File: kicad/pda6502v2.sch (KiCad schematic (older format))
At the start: 85 parts, among them J1 GPIO1, J2 GPIO2, J3 UART, J4 Screw_Terminal_01x02, J5 Conn_02x04_Odd_Even, J6 ICSP, J7 SPI, J8 FPGA_EXT, J9 SID, SW1 SW_Push, U1 W65C02SxP, U10 LT3030, U11 SC28L92A1B, U2 W65C22SxP, U3 W65C22SxP, U4 DS1818, U5 AS6C4008-55PCN, U6 ARMSID, U7 AT25M01, U8 ICE40HX4K-TQ144, U9 TLV1117-33, X1 8 MHz, X2 3.6864 MHz

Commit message: Routing WIP; UART
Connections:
- net UART_RXA~IRQ: now also U8.98 (IOR_148); no longer U8.99 (IOR_152)
- net UART_TXA~IRQ: now also U8.97 (IOR_147); no longer U8.98 (IOR_148)
- net UART_~CS: now also U8.99 (IOR_152); no longer U8.97 (IOR_147)
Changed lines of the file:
@@
 Text Label 11750 5550 2    50   ~ 0
 UART_TXB~IRQ
-Text Label 11750 6050 2    50   ~ 0
+Text Label 11750 5950 2    50   ~ 0
 UART_TXA~IRQ
 Text Label 11750 5650 2    50   ~ 0
 UART_RXB~IRQ
-Text Label 11750 6150 2    50   ~ 0
+Text Label 11750 6050 2    50   ~ 0
 UART_RXA~IRQ
 Text Label 11750 5750 2    50   ~ 0
@@
 Text Label 14750 4950 2    50   ~ 0
 RAM_~CS
-Text Label 11750 5950 2    50   ~ 0
+Text Label 11750 6150 2    50   ~ 0
 UART_~CS
 Text Label 11750 6750 2    50   ~ 0

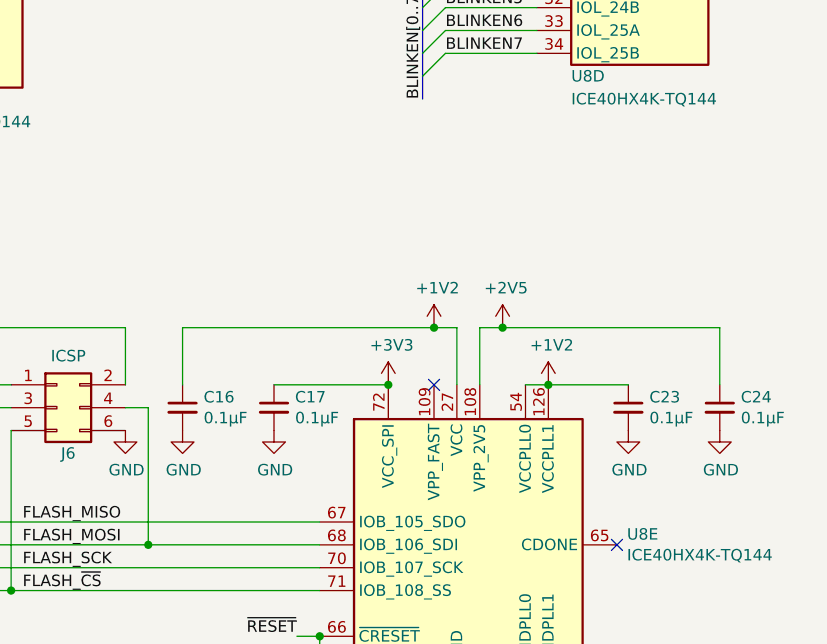
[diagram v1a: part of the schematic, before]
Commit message: LDO placement/routing, XO HandSolder footprint, etc.
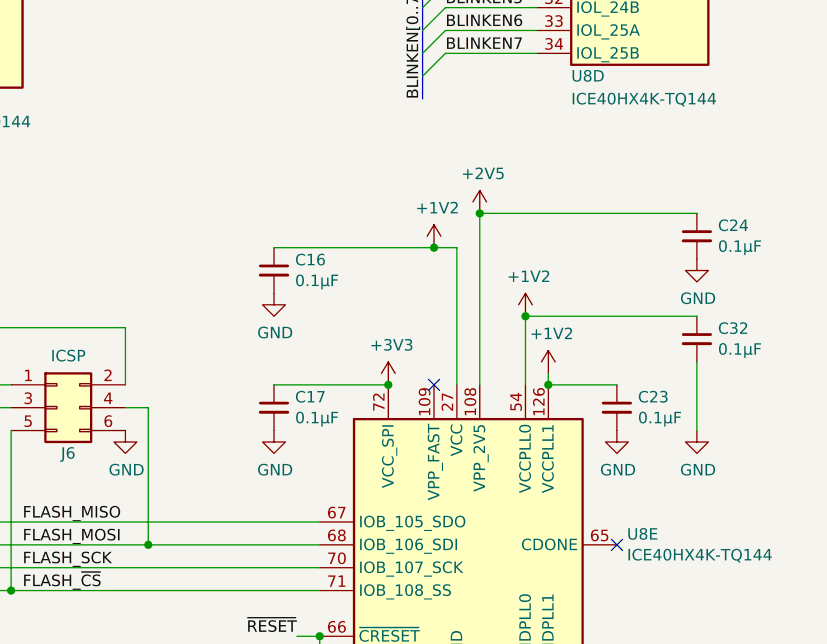
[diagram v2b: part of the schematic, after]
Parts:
- added C32: 0.1μF, Capacitor_SMD:C_0805_2012Metric_Pad1.18x1.45mm_HandSolder, symbol Device:C_Small
- X1, X2: footprint Oscillator:Oscillator_SMD_EuroQuartz_XO53-4Pin_5.0x3.2mm -> pda6502v2:Oscillator_SMD_5.0x3.2mm_HandSolder
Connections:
- net +1V2: now also C32.1
- net GND: now also C32.2
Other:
- moved on the sheet: C16, C23, C24
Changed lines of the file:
@@
 UART_IM
 Wire Wire Line
-	14600 7850 15550 7850
-Wire Wire Line
-	15550 7850 15550 8100
-Wire Wire Line
-	13200 7850 14300 7850
-Wire Wire Line
-	13200 7850 13200 8100
+	14500 7350 15450 7350
+Wire Wire Line
+	13600 7500 14300 7500
 $Comp
 L power:GND #PWR079
 U 1 1 61F81ED6
-P 15550 8300
-F 0 "#PWR079" H 15550 8050 50  0001 C CNN
-F 1 "GND" H 15555 8127 50  0000 C CNN
-F 2 "" H 15550 8300 50  0001 C CNN
-F 3 "" H 15550 8300 50  0001 C CNN
-	1    15550 8300
+P 15450 7550
+F 0 "#PWR079" H 15450 7300 50  0001 C CNN
+F 1 "GND" H 15455 7377 50  0000 C CNN
+F 2 "" H 15450 7550 50  0001 C CNN
+F 3 "" H 15450 7550 50  0001 C CNN
+	1    15450 7550
 	1    0    0    -1
 $EndComp
@@
 L Device:C_Small C24
 U 1 1 61F81ECC
-P 15550 8200
-F 0 "C24" H 15642 8246 50  0000 L CNN
-F 1 "0.1μF" H 15642 8155 50  0000 L CNN
-F 2 "Capacitor_SMD:C_0805_2012Metric_Pad1.18x1.45mm_HandSolder" H 15550 8200 50  0001 C CNN
-F 3 "~" H 15550 8200 50  0001 C CNN
-	1    15550 8200
-	1    0    0    -1
-$EndComp
-Connection ~ 14600 7850
-Connection ~ 14300 7850
-Wire Wire Line
-	14400 7850 14300 7850
-Wire Wire Line
-	14400 8100 14400 7850
-Wire Wire Line
-	14500 7850 14600 7850
-Wire Wire Line
-	14500 8100 14500 7850
-Wire Wire Line
-	14800 8100 15150 8100
+P 15450 7450
+F 0 "C24" H 15542 7496 50  0000 L CNN
+F 1 "0.1μF" H 15542 7405 50  0000 L CNN
+F 2 "Capacitor_SMD:C_0805_2012Metric_Pad1.18x1.45mm_HandSolder" H 15450 7450 50  0001 C CNN
+F 3 "~" H 15450 7450 50  0001 C CNN
+	1    15450 7450
+	1    0    0    -1
+$EndComp
+Connection ~ 14500 7350
+Connection ~ 14300 7500
+Wire Wire Line
+	14400 7500 14300 7500
+Wire Wire Line
+	14400 8100 14400 7500
+Wire Wire Line
+	14500 8100 14500 7350
 $Comp
 L power:GND #PWR077
 U 1 1 61D7E730
-P 15150 8300
-F 0 "#PWR077" H 15150 8050 50  0001 C CNN
-F 1 "GND" H 15155 8127 50  0000 C CNN
-F 2 "" H 15150 8300 50  0001 C CNN
-F 3 "" H 15150 8300 50  0001 C CNN
-	1    15150 8300
+P 15100 8300
+F 0 "#PWR077" H 15100 8050 50  0001 C CNN
+F 1 "GND" H 15105 8127 50  0000 C CNN
+F 2 "" H 15100 8300 50  0001 C CNN
+F 3 "" H 15100 8300 50  0001 C CNN
+	1    15100 8300
 	1    0    0    -1
 $EndComp
@@
 L Device:C_Small C23
 U 1 1 61D7E726
-P 15150 8200
-F 0 "C23" H 15242 8246 50  0000 L CNN
-F 1 "0.1μF" H 15242 8155 50  0000 L CNN
-F 2 "Capacitor_SMD:C_0805_2012Metric_Pad1.18x1.45mm_HandSolder" H 15150 8200 50  0001 C CNN
-F 3 "~" H 15150 8200 50  0001 C CNN
-	1    15150 8200
-	1    0    0    -1
-$EndComp
-Connection ~ 14800 8100
-Wire Wire Line
-	14700 8100 14800 8100
+P 15100 8200
+F 0 "C23" H 15192 8246 50  0000 L CNN
+F 1 "0.1μF" H 15192 8155 50  0000 L CNN
+F 2 "Capacitor_SMD:C_0805_2012Metric_Pad1.18x1.45mm_HandSolder" H 15100 8200 50  0001 C CNN
+F 3 "~" H 15100 8200 50  0001 C CNN
+	1    15100 8200
+	1    0    0    -1
+$EndComp
 $Comp
 L power:GND #PWR060
 U 1 1 61C44B47
-P 13200 8300
-F 0 "#PWR060" H 13200 8050 50  0001 C CNN
-F 1 "GND" H 13205 8127 50  0000 C CNN
-F 2 "" H 13200 8300 50  0001 C CNN
-F 3 "" H 13200 8300 50  0001 C CNN
-	1    13200 8300
+P 13600 7700
+F 0 "#PWR060" H 13600 7450 50  0001 C CNN
+F 1 "GND" H 13605 7527 50  0000 C CNN
+F 2 "" H 13600 7700 50  0001 C CNN
+F 3 "" H 13600 7700 50  0001 C CNN
+	1    13600 7700
 	1    0    0    -1
 $EndComp
@@
 L Device:C_Small C16
 U 1 1 61C44B3D
-P 13200 8200
-F 0 "C16" H 13292 8246 50  0000 L CNN
-F 1 "0.1μF" H 13292 8155 50  0000 L CNN
-F 2 "Capacitor_SMD:C_0805_2012Metric_Pad1.18x1.45mm_HandSolder" H 13200 8200 50  0001 C CNN
-F 3 "~" H 13200 8200 50  0001 C CNN
-	1    13200 8200
+P 13600 7600
+F 0 "C16" H 13692 7646 50  0000 L CNN
+F 1 "0.1μF" H 13692 7555 50  0000 L CNN
+F 2 "Capacitor_SMD:C_0805_2012Metric_Pad1.18x1.45mm_HandSolder" H 13600 7600 50  0001 C CNN
+F 3 "~" H 13600 7600 50  0001 C CNN
+	1    13600 7600
 	1    0    0    -1
 $EndComp
@@
 L power:+1V2 #PWR?
 U 1 1 609BB90F
-P 14800 8100
+P 14800 8050
 AR Path="/609162A8/609BB90F" Ref="#PWR?"  Part="1"
 AR Path="/609BB90F" Ref="#PWR075"  Part="1"
-F 0 "#PWR075" H 14800 7950 50  0001 C CNN
-F 1 "+1V2" H 14815 8273 50  0000 C CNN
-F 2 "" H 14800 8100 50  0001 C CNN
-F 3 "" H 14800 8100 50  0001 C CNN
-	1    14800 8100
+F 0 "#PWR075" H 14800 7900 50  0001 C CNN
+F 1 "+1V2" H 14815 8223 50  0000 C CNN
+F 2 "" H 14800 8050 50  0001 C CNN
+F 3 "" H 14800 8050 50  0001 C CNN
+	1    14800 8050
 	1    0    0    -1
 $EndComp
@@
 L power:+1V2 #PWR?
 U 1 1 609BB906
-P 14300 7850
+P 14300 7500
 AR Path="/609162A8/609BB906" Ref="#PWR?"  Part="1"
 AR Path="/609BB906" Ref="#PWR068"  Part="1"
-F 0 "#PWR068" H 14300 7700 50  0001 C CNN
-F 1 "+1V2" H 14315 8023 50  0000 C CNN
-F 2 "" H 14300 7850 50  0001 C CNN
-F 3 "" H 14300 7850 50  0001 C CNN
-	1    14300 7850
+F 0 "#PWR068" H 14300 7350 50  0001 C CNN
+F 1 "+1V2" H 14315 7673 50  0000 C CNN
+F 2 "" H 14300 7500 50  0001 C CNN
+F 3 "" H 14300 7500 50  0001 C CNN
+	1    14300 7500
 	1    0    0    -1
 $EndComp
@@
 L power:+2V5 #PWR?
 U 1 1 609BB900
-P 14600 7850
+P 14500 7350
 AR Path="/609162A8/609BB900" Ref="#PWR?"  Part="1"
 AR Path="/609BB900" Ref="#PWR070"  Part="1"
-F 0 "#PWR070" H 14600 7700 50  0001 C CNN
-F 1 "+2V5" H 14615 8023 50  0000 C CNN
-F 2 "" H 14600 7850 50  0001 C CNN
-F 3 "" H 14600 7850 50  0001 C CNN
-	1    14600 7850
+F 0 "#PWR070" H 14500 7200 50  0001 C CNN
+F 1 "+2V5" H 14515 7523 50  0000 C CNN
+F 2 "" H 14500 7350 50  0001 C CNN
+F 3 "" H 14500 7350 50  0001 C CNN
+	1    14500 7350
 	1    0    0    -1
 $EndComp
@@
 F 0 "X1" H 6544 1746 50  0000 L CNN
 F 1 "8 MHz" H 6544 1655 50  0000 L CNN
-F 2 "Oscillator:Oscillator_SMD_EuroQuartz_XO53-4Pin_5.0x3.2mm" H 6900 1350 50  0001 C CNN
+F 2 "pda6502v2:Oscillator_SMD_5.0x3.2mm_HandSolder" H 6900 1350 50  0001 C CNN
 F 3 "https://abracon.com/Oscillators/ASFL1.pdf" H 6100 1700 50  0001 C CNN
 	1    6200 1700
@@
 F 0 "X2" H 1344 5846 50  0000 L CNN
 F 1 "3.6864 MHz" H 1344 5755 50  0000 L CNN
-F 2 "Oscillator:Oscillator_SMD_EuroQuartz_XO53-4Pin_5.0x3.2mm" H 1700 5450 50  0001 C CNN
+F 2 "pda6502v2:Oscillator_SMD_5.0x3.2mm_HandSolder" H 1700 5450 50  0001 C CNN
 F 3 "https://abracon.com/Oscillators/ASFL1.pdf" H 900 5800 50  0001 C CNN
 	1    1000 5800
@@
 NoConn ~ 14750 5250
 NoConn ~ 14750 5550
+$Comp
+L Device:C_Small C32
+U 1 1 613A4B5A
+P 15450 7900
+F 0 "C32" H 15542 7946 50  0000 L CNN
+F 1 "0.1μF" H 15542 7855 50  0000 L CNN
+F 2 "Capacitor_SMD:C_0805_2012Metric_Pad1.18x1.45mm_HandSolder" H 15450 7900 50  0001 C CNN
+F 3 "~" H 15450 7900 50  0001 C CNN
+	1    15450 7900
+	1    0    0    -1
+$EndComp
+$Comp
+L power:+1V2 #PWR?
+U 1 1 613A5980
+P 14700 7800
+AR Path="/609162A8/613A5980" Ref="#PWR?"  Part="1"
+AR Path="/613A5980" Ref="#PWR036"  Part="1"
+F 0 "#PWR036" H 14700 7650 50  0001 C CNN
+F 1 "+1V2" H 14715 7973 50  0000 C CNN
+F 2 "" H 14700 7800 50  0001 C CNN
+F 3 "" H 14700 7800 50  0001 C CNN
+	1    14700 7800
+	1    0    0    -1
+$EndComp
+Wire Wire Line
+	14800 8100 15100 8100
+$Comp
+L power:GND #PWR037
+U 1 1 61A42391
+P 15450 8300
+F 0 "#PWR037" H 15450 8050 50  0001 C CNN
+F 1 "GND" H 15455 8127 50  0000 C CNN
+F 2 "" H 15450 8300 50  0001 C CNN
+F 3 "" H 15450 8300 50  0001 C CNN
+	1    15450 8300
+	1    0    0    -1
+$EndComp
+Wire Wire Line
+	14700 8100 14700 7800
+Wire Wire Line
+	14700 7800 15450 7800
+Connection ~ 14700 7800
+Wire Wire Line
+	14800 8100 14800 8050
+Connection ~ 14800 8100
+Wire Wire Line
+	15450 8300 15450 8000
 Wire Bus Line
 	6500 5450 6500 5900

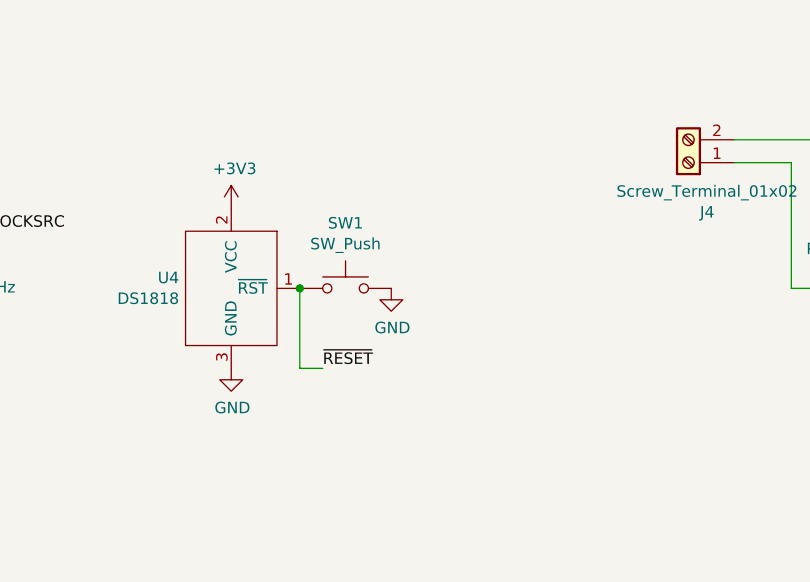
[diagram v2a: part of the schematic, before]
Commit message: Routing; power, ground vias, UART/osc, reset button/header, etc.
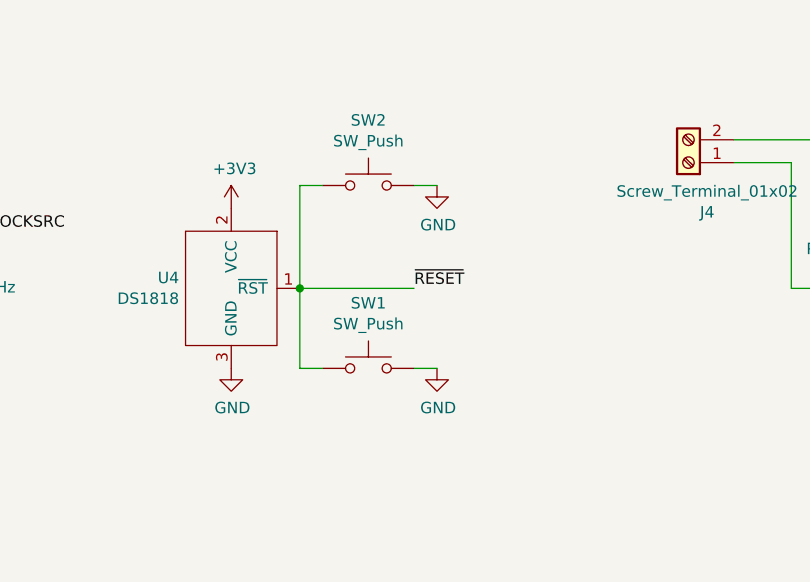
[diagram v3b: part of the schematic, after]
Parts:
- added SW2: SW_Push, Connector_PinHeader_2.54mm:PinHeader_1x02_P2.54mm_Vertical, symbol Switch:SW_Push
- SW1: footprint Button_Switch_THT:SW_Tactile_Straight_KSA0Axx1LFTR -> Button_Switch_THT:SW_PUSH_6mm_H5mm
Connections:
- net GND: now also SW2.1
- net ~RESET: now also SW2.2
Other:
- moved on the sheet: SW1
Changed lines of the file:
@@
 L power:GND #PWR025
 U 1 1 60C137D1
-P 8400 1750
-F 0 "#PWR025" H 8400 1500 50  0001 C CNN
-F 1 "GND" H 8405 1577 50  0000 C CNN
-F 2 "" H 8400 1750 50  0001 C CNN
-F 3 "" H 8400 1750 50  0001 C CNN
-	1    8400 1750
+P 8600 2100
+F 0 "#PWR025" H 8600 1850 50  0001 C CNN
+F 1 "GND" H 8605 1927 50  0000 C CNN
+F 2 "" H 8600 2100 50  0001 C CNN
+F 3 "" H 8600 2100 50  0001 C CNN
+	1    8600 2100
 	1    0    0    -1
 $EndComp
@@
 L Switch:SW_Push SW1
 U 1 1 60C12C39
-P 8200 1750
-F 0 "SW1" H 8200 2035 50  0000 C CNN
-F 1 "SW_Push" H 8200 1944 50  0000 C CNN
-F 2 "Button_Switch_THT:SW_Tactile_Straight_KSA0Axx1LFTR" H 8200 1950 50  0001 C CNN
-F 3 "~" H 8200 1950 50  0001 C CNN
-	1    8200 1750
+P 8300 2100
+F 0 "SW1" H 8300 2385 50  0000 C CNN
+F 1 "SW_Push" H 8300 2294 50  0000 C CNN
+F 2 "Button_Switch_THT:SW_PUSH_6mm_H5mm" H 8300 2300 50  0001 C CNN
+F 3 "~" H 8300 2300 50  0001 C CNN
+	1    8300 2100
 	1    0    0    -1
 $EndComp
-Text Label 8100 2100 0    50   ~ 0
-~RESET
 Wire Wire Line
 	8000 1750 8000 2100
@@
 Wire Wire Line
 	15450 8300 15450 8000
+$Comp
+L Switch:SW_Push SW2
+U 1 1 624A3E44
+P 8300 1300
+F 0 "SW2" H 8300 1585 50  0000 C CNN
+F 1 "SW_Push" H 8300 1494 50  0000 C CNN
+F 2 "Connector_PinHeader_2.54mm:PinHeader_1x02_P2.54mm_Vertical" H 8300 1500 50  0001 C CNN
+F 3 "~" H 8300 1500 50  0001 C CNN
+	1    8300 1300
+	-1   0    0    -1
+$EndComp
+$Comp
+L power:GND #PWR0123
+U 1 1 6251079F
+P 8600 1300
+F 0 "#PWR0123" H 8600 1050 50  0001 C CNN
+F 1 "GND" H 8605 1127 50  0000 C CNN
+F 2 "" H 8600 1300 50  0001 C CNN
+F 3 "" H 8600 1300 50  0001 C CNN
+	1    8600 1300
+	1    0    0    -1
+$EndComp
+Wire Wire Line
+	8500 1300 8600 1300
+Wire Wire Line
+	8500 2100 8600 2100
+Wire Wire Line
+	8000 1750 8500 1750
+Text Label 8500 1750 0    50   ~ 0
+~RESET
+Wire Wire Line
+	8000 1300 8100 1300
+Wire Wire Line
+	8000 1300 8000 1750
 Wire Bus Line
 	6500 5450 6500 5900

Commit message: BLINKEN and other minor tweaks
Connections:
- net VCC_FLASH: now reaches C10.1, D11.1 (K), J6.2 (Pin_2), U7.3 (~WP), U7.7 (~HOLD), U7.8 (VCC)
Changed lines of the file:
@@
 	8000 1300 8000 1750
+Wire Bus Line
+	6600 6250 6600 7000
 Wire Bus Line
 	6500 5450 6500 5900
 Wire Bus Line
+	5100 9750 5100 10500
+Wire Bus Line
 	4900 9050 4900 9400
-Wire Bus Line
-	1650 4700 1650 5050
-Wire Bus Line
-	900  9050 900  9400
-Wire Bus Line
-	6600 6250 6600 7000
-Wire Bus Line
-	5100 9750 5100 10500
 Wire Bus Line
 	14250 6050 14250 6850
@@
 	9850 5700 9850 6450
 Wire Bus Line
+	9950 3750 9950 5650
+Wire Bus Line
 	1650 6200 1650 6950
+Wire Bus Line
+	1650 4700 1650 5050
+Wire Bus Line
+	2750 1000 2750 2550
+Wire Bus Line
+	3600 1200 3600 3100
 Wire Bus Line
 	5150 950  5150 1700
@@
 	1100 9750 1100 10500
 Wire Bus Line
+	900  9050 900  9400
+Wire Bus Line
 	2750 2950 2750 3700
-Wire Bus Line
-	2750 1000 2750 2550
-Wire Bus Line
-	3600 1200 3600 3100
-Wire Bus Line
-	9950 3750 9950 5650
+Text Label 12950 7850 2    50   ~ 0
+VCC_FLASH
 $EndSCHEMATC
